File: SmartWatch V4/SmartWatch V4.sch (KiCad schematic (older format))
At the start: 44 parts

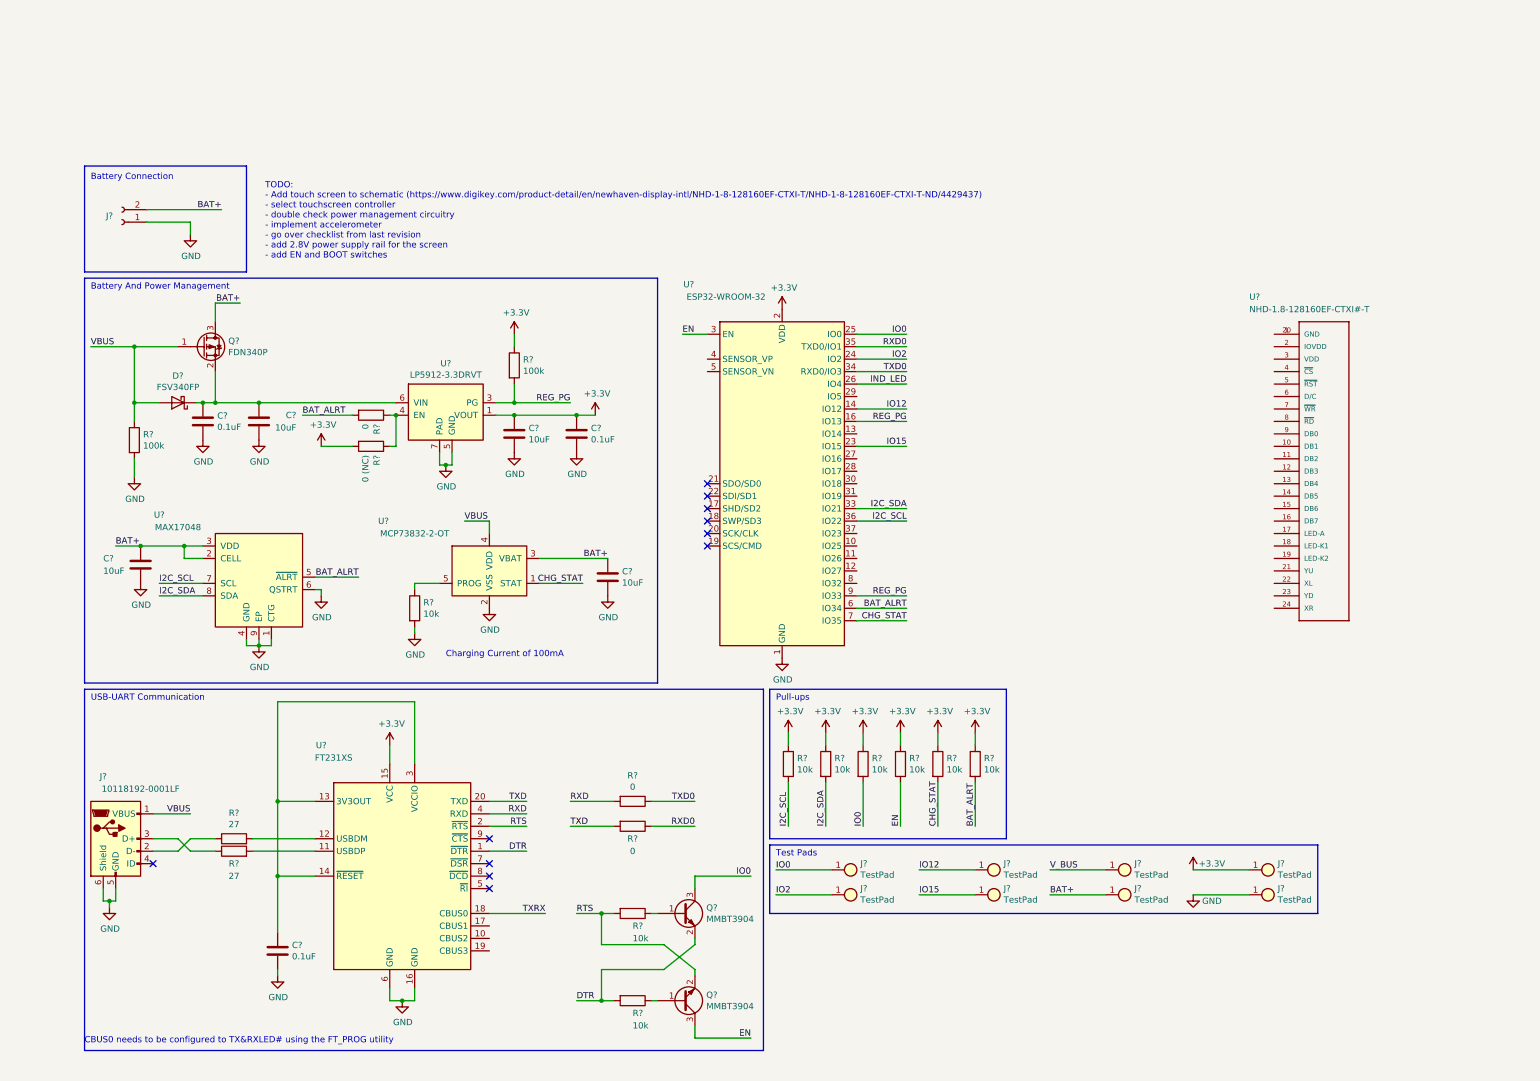
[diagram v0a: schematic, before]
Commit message: Connected LCD and LCD power source
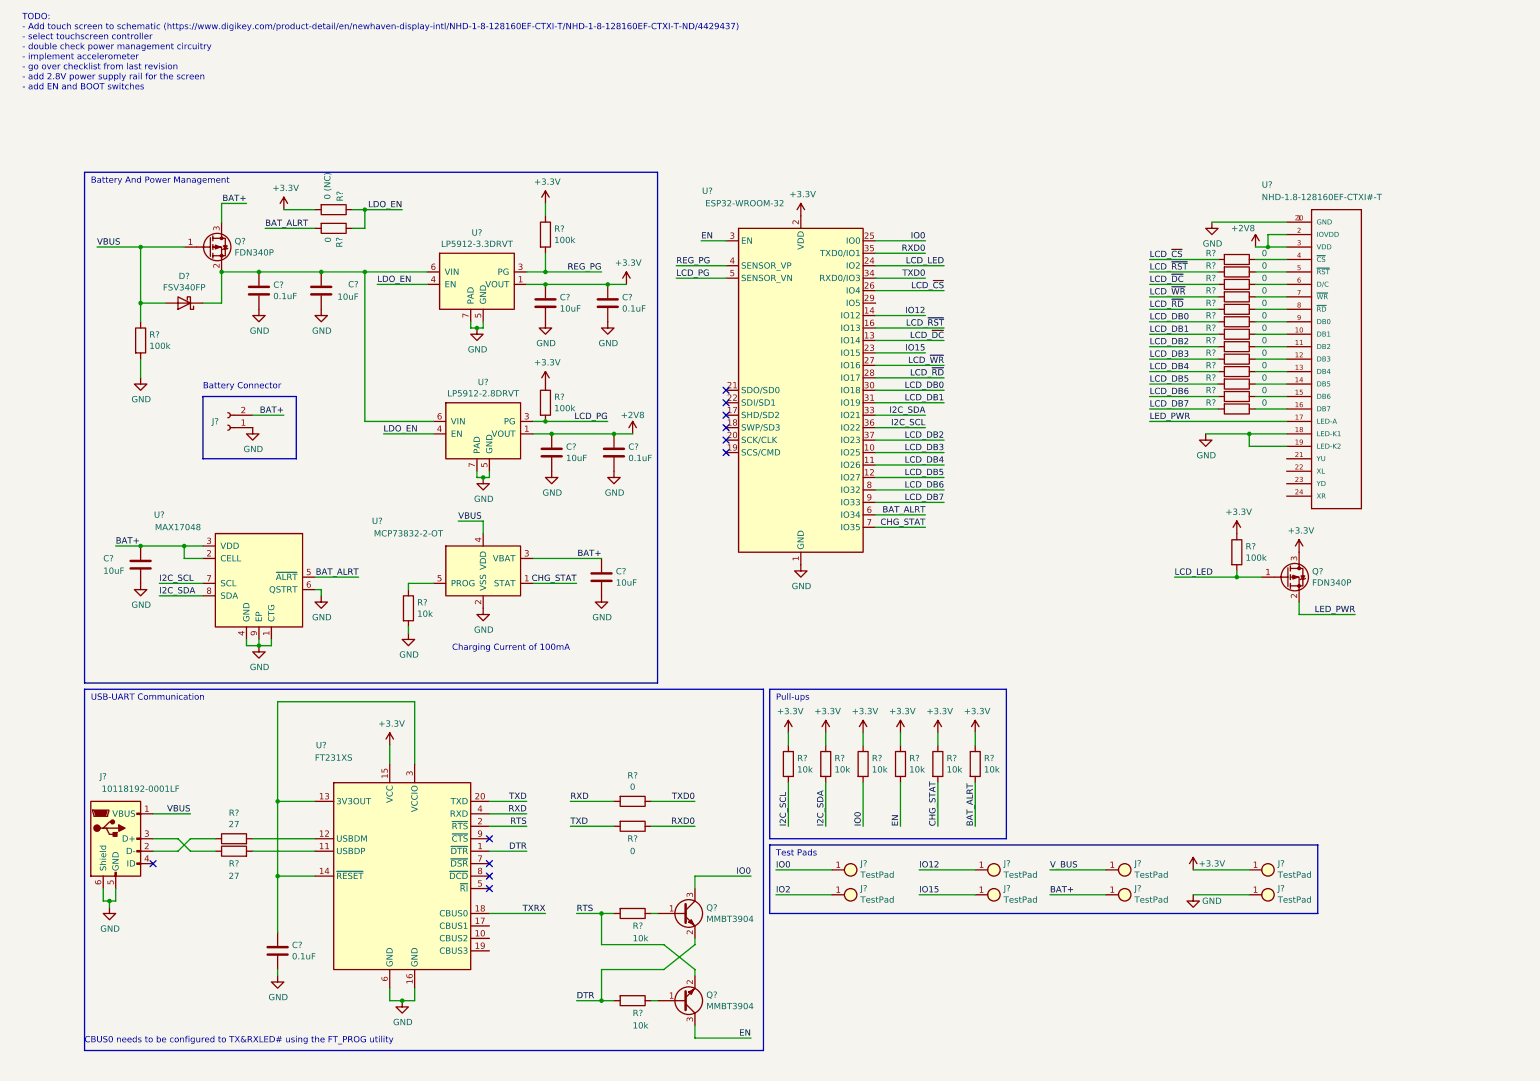
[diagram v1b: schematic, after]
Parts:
- added C?: 0.1uF, symbol Device:C
- added C?: 10uF, Capacitor_SMD:C_0603_1608Metric, symbol Device:C
- added Q?: FDN340P, Package_TO_SOT_SMD:SOT-23, symbol Device:Q_PMOS_GSD
- added R? (x2): 100k, Resistor_SMD:R_0603_1608Metric, symbol Device:R
- added R? (x13): 0, Resistor_SMD:R_0603_1608Metric, symbol Device:R
- added U?: LP5912-2.8DRVT, Package_SON:WSON-6-1EP_2x2mm_P0.65mm_EP1x1.6mm_ThermalVias, symbol CustomParts:LP5912-3.3DRVT
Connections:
- net +3V3: now also Q?.3 (D), R?.1, R?.1
- net GND: now also U?.1 (GND), U?.18 (LED‐K1), U?.19 (LED‐K2), U?.20 (GND), C?.2, C?.2, U?.5 (GND), U?.7 (PAD)
- net IO2: no longer U?.24 (IO2)
- net REG_PG: now also U?.4 (SENSOR_VP); no longer U?.16 (IO13), U?.9 (IO33)
- net LCD_DB3: now reaches U?.10 (IO25)
- net LCD_DB3: now also R?.2
- net LCD_DB4: now reaches U?.11 (IO26)
- net LCD_DB4: now also R?.2
- net LCD_DB5: now reaches U?.12 (IO27)
- net LCD_DB5: now also R?.2
- net LCD_~DC~: now reaches U?.13 (IO14)
- net LCD_~DC~: now also R?.2
- net LCD_~WR~: now reaches U?.27 (IO16)
- net LCD_~WR~: now also R?.2
- net LCD_~RD~: now reaches U?.28 (IO17)
- net LCD_~RD~: now also R?.2
- net LCD_DB0: now reaches U?.30 (IO18)
- net LCD_DB0: now also R?.2
- net LCD_DB1: now reaches U?.31 (IO19)
- net LCD_DB1: now also R?.2
- net LCD_DB2: now reaches U?.37 (IO23)
- net LCD_DB2: now also R?.2
- net LCD_PG: now reaches U?.5 (SENSOR_VN)
- net LCD_PG: now also R?.2, U?.3 (PG~)
- net LCD_DB6: now reaches U?.8 (IO32)
- net LCD_DB6: now also R?.2
- net at U?.10 (DB1): now also R?.1
- net at U?.11 (DB2): now also R?.1
- net at U?.12 (DB3): now also R?.1
- net at U?.13 (DB4): now also R?.1
- net at U?.14 (DB5): now also R?.1
- net at U?.15 (DB6): now also R?.1
- net at U?.16 (DB7): now also R?.1
- net LED_PWR: now reaches U?.17 (LED‐A)
- net LED_PWR: now also Q?.2 (S)
- net +2V8: now reaches U?.2 (IOVDD)
- net +2V8: now also U?.3 (VDD), C?.1, C?.1, U?.1 (VOUT)
- net at U?.4 (~CS~): now also R?.1
- net at U?.5 (~RST~): now also R?.1
- net at U?.6 (D/C): now also R?.1
- net at U?.7 (~WR~): now also R?.1
- net at U?.8 (~RD~): now also R?.1
- net at U?.9 (DB0): now also R?.1
- net at C?.1, C?.1, D?.1 (K)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: now also U?.6 (VIN)
- net LDO_EN: now reaches R?.1, R?.1, U?.4 (EN)
- net LDO_EN: now also U?.4 (EN)
- net IND_LED renamed LCD_~CS~
- net LCD_~CS~: now also R?.2
- new net LCD_DB7: R?.2, U?.9 (IO33)
- new net LCD_LED: Q?.1 (G), R?.2, U?.24 (IO2)
- new net LCD_~RST~: R?.2, U?.16 (IO13)
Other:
- note added: "Battery Connector"
- note removed: "Battery Connection\n\n"
- moved on the sheet: C?, D?, J?, Q?, R?, U?

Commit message: Completed Implementation of Touch Screen
TODO: Final checks on circuit design
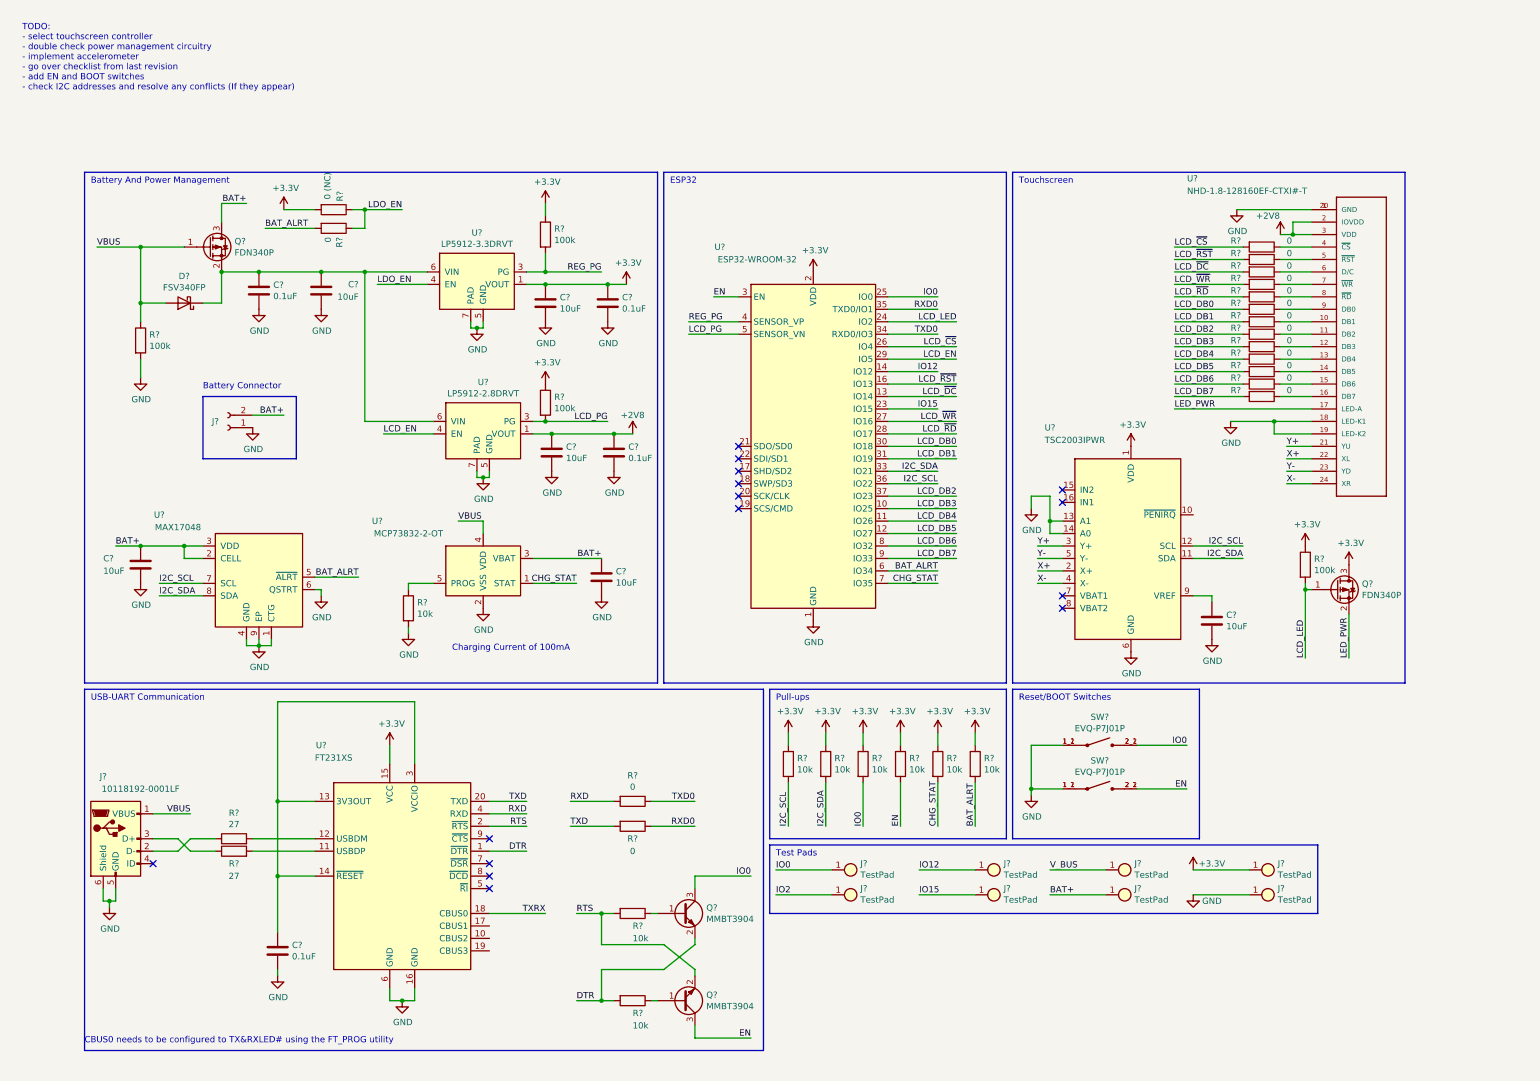
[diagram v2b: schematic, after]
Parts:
- added C?: 10uF, Capacitor_SMD:C_0603_1608Metric, symbol Device:C
- added SW? (x2): EVQ-P7J01P, CustomFootprints:SW_EVQ-P7J01P, symbol CustomParts:EVQ-P7J01P
- added U?: TSC2003IPWR, Package_SO:TSSOP-16_4.4x5mm_P0.65mm, symbol CustomParts:TSC2003IPWR
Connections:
- net +3V3: now also U?.1 (VDD)
- net EN: now also SW?.2_1 (2), SW?.2_2 (2)
- net GND: now also C?.2, SW?.1_1 (1), SW?.1_1 (1), SW?.1_2 (1), SW?.1_2 (1), U?.13 (A1), U?.14 (A0), U?.6 (GND)
- net I2C_SCL: now also U?.12 (SCL)
- net I2C_SDA: now also U?.11 (SDA)
- net IO0: now also SW?.2_1 (2), SW?.2_2 (2)
- net LDO_EN: no longer U?.4 (EN)
- net LCD_EN: now reaches U?.29 (IO5)
- net LCD_EN: now also U?.4 (EN)
- net Y+: now reaches U?.21 (YU)
- net Y+: now also U?.3 (Y+)
- net X+: now reaches U?.22 (XL)
- net X+: now also U?.2 (X+)
- net Y-: now reaches U?.23 (YD)
- net Y-: now also U?.5 (Y-)
- net X-: now reaches U?.24 (XR)
- net X-: now also U?.4 (X-)
- new net: C?.1, U?.9 (VREF)
- no-connect marks 11 -> 15
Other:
- note added: "ESP32"
- note added: "Reset/BOOT Switches"
- note added: "TODO: \n- select touchscreen controller\n- double check power management circuitry\n- implement accelerometer\n- go over checklist from last revision\n- add EN and BOOT switches\n- check I2C addresses and resolve any conflicts (If they appear)\n"
- note added: "Touchscreen"
- note removed: "TODO: \n- Add touch screen to schematic (https://www.digikey.com/product-detail/en/newhaven-display-intl/NHD-1-8-128160EF-CTXI-T/NHD-1-8-128160EF-CTXI-T-ND/4429437)\n- select touchscreen controller\n- double check power management circuitry\n- implement accelerometer\n- go over checklist from last revision\n- add 2.8V power supply rail for the screen\n- add EN and BOOT switches"
- moved on the sheet: Q?, R?, U?

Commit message: minor edits
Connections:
- net IO15: no longer U?.23 (IO15)
- net LCD_LED: now also U?.23 (IO15); no longer U?.24 (IO2)
- no-connect marks 15 -> 16
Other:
- note added: "TODO: \n- double check power management circuitry\n- go over checklist from last revision\n- double check NC on IN1 and IN2 of touch controller\n- attach touch interrupt pin to ESP32 RTC pin\n- check I2C addresses and resolve any conflicts (If they appear)\n"
- note removed: "TODO: \n- select touchscreen controller\n- double check power management circuitry\n- implement accelerometer\n- go over checklist from last revision\n- add EN and BOOT switches\n- check I2C addresses and resolve any conflicts (If they appear)\n"

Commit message: Completed Electrical Schematic
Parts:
- removed R? (x13): 0, Resistor_SMD:R_0603_1608Metric, symbol Device:R
- added J? (x4): TestPad, CustomFootprints:TESTPAD, symbol CustomParts:TestPad
- added R19: 10k, symbol Device:R
- added R20, R21: 100k, Resistor_SMD:R_0603_1608Metric, symbol Device:R
- added U7, U8, U9: NLSV4T244, CustomFootprints:NLSV4T244MUTAG, symbol CustomParts:NLSV4T244
- gave numbers to parts that had none: 54
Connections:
- net LCD_LED is gone; now on net IO15: Q4.1 (G), R22.2, U6.23 (IO15)
- net LCD_~CS~ is gone; now on net TOUCH_IRQ: U6.26 (IO4)
- net V_BUS is gone; now on net VBUS: J7.1
- net +2V8: now also R20.1, U7.11 (VCCB), U8.11 (VCCB), U9.11 (VCCB)
- net +3V3: now also R21.1, U7.1 (VCCA), U8.1 (VCCA), U9.1 (VCCA)
- net GND: now also R19.2, U7.12 (~OE), U7.6 (GND), U8.12 (~OE), U8.6 (GND), U9.12 (~OE), U9.6 (GND)
- net IO12: now also R19.1, U7.2 (A1)
- net IO2: now also U6.24 (IO2)
- net LCD_DB0: now also U8.2 (A1)
- net LCD_DB1: now also U8.3 (A2)
- net LCD_DB2: now also U8.4 (A3)
- net LCD_DB3: now also U8.5 (A4)
- net LCD_DB4: now also U9.2 (A1)
- net LCD_DB5: now also U9.3 (A2)
- net LCD_DB6: now also U9.4 (A3)
- net LCD_DB7: now also U9.5 (A4)
- net LCD_~DC~: now also U7.3 (A2)
- net LCD_~RD~: now also U7.5 (A4)
- net LCD_~RST~: now also U11.5 (~RST~), R20.2
- net LCD_~WR~: now also U7.4 (A3)
- net at U2.10 (CBUS2): now also J?.1
- net at U2.17 (CBUS1): now also J?.1
- net at U2.19 (CBUS3): now also J?.1
- net at U11.10 (DB1): now also U8.9 (B2)
- net at U11.11 (DB2): now also U8.8 (B3)
- net at U11.12 (DB3): now also U8.7 (B4)
- net at U11.13 (DB4): now also U9.10 (B1)
- net at U11.14 (DB5): now also U9.9 (B2)
- net at U11.15 (DB6): now also U9.8 (B3)
- net at U11.16 (DB7): now also U9.7 (B4)
- net at U11.4 (~CS~): now also U7.10 (B1)
- net at U11.6 (D/C): now also U7.9 (B2)
- net at U11.7 (~WR~): now also U7.8 (B3)
- net at U11.8 (~RD~): now also U7.7 (B4)
- net at U11.9 (DB0): now also U8.10 (B1)
- net TOUCH_IRQ: now reaches U10.10 (~PENIRQ~)
- net TOUCH_IRQ: now also R21.2
- net TXRX: no longer names the net of U2.18 (CBUS0)
- net TXRX: now also J?.1
- no-connect marks 16 -> 15
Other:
- note added: "NOTE: LCD_RST should only be set to either LOW or HIGH-Z\n"
- note added: "TODO: \n- double check power management circuitry\n- go over checklist from last revision\n- check I2C addresses and resolve any conflicts (If they appear)\n"
- note removed: "TODO: \n- double check power management circuitry\n- go over checklist from last revision\n- double check NC on IN1 and IN2 of touch controller\n- attach touch interrupt pin to ESP32 RTC pin\n- check I2C addresses and resolve any conflicts (If they appear)\n"
- moved on the sheet: C10, J10, J3, J4, J5, J6, J7, J8, J9, Q2, Q3, Q4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

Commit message: assigned all footprints to components
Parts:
- C3, C8, C9: footprint (none) -> Capacitor_SMD:C_0603_1608Metric
- R10, R13, R14, R15, R16, R17, R18, R19, R9: footprint (none) -> Resistor_SMD:R_0603_1608Metric
- R11, R12: footprint Resistor_SMD:R_0805_2012Metric -> Resistor_SMD:R_0603_1608Metric
- U11: footprint LCD_NHD-1.8-128160EF-CTXI#-T -> CustomFootprints:LCD_NHD-1.8-128160EF-CTXI#-T
- gave numbers to parts that had none: 4
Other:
- note added: "TODO: \n- double check power management circuitry\n- go over checklist from last revision"
- note removed: "TODO: \n- double check power management circuitry\n- go over checklist from last revision\n- check I2C addresses and resolve any conflicts (If they appear)\n"

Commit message: minor edits
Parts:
- C2: footprint (none) -> Capacitor_SMD:C_0603_1608Metric
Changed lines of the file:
@@
 F 0 "C2" H 2065 1546 50  0000 L CNN
 F 1 "0.1uF" H 2065 1455 50  0000 L CNN
-F 2 "" H 1988 1350 50  0001 C CNN
+F 2 "Capacitor_SMD:C_0603_1608Metric" H 1988 1350 50  0001 C CNN
 F 3 "~" H 1950 1500 50  0001 C CNN
 F 4 "1276-1006-1-ND" H 1950 1500 50  0001 C CNN "digikey"
